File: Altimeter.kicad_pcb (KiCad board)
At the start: 4 copper layers, 37.5 x 25 mm, 99 parts, among them IC1 XTSD02GLGEAG, J1 Conn_01x04_Male, J2 Conn_01x02_Male, J3 USB_C_Receptacle_USB2.0, J4 Conn_01x02_Male, Q1 PMV20ENR, U1 150044M155220, U10 MAX77827AEFD+T, U11 SC4215, U2 ESP32-S3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

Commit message: 3rd iteration
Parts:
- added TP7: TestPoint, TestPoint:TestPoint_Pad_D1.0mm, B.Cu at (110.7, 97.8)
- USBLED1: footprint LED_SMD:LED_0603_1608Metric -> LED_SMD:LED_0402_1005Metric
- moved G*** 8.72 mm to (110.1, 90.9)
- moved USBLED1 8.01 mm to (128.3, 102.7), turned to 180 degrees
- moved TP5 3.57 mm to (106.4, 108.4)
- moved C14 3.19 mm to (107.0, 87.0), turned to 90 degrees
- moved R9 2.93 mm to (111.5, 89.5)
- moved R14 2.72 mm to (126.4, 102.7), turned to 0 degrees
- moved C13 2.39 mm to (110.9, 87.1)
- moved C1 2.19 mm to (103.7, 85.8), turned to 180 degrees
- moved TP9 1.98 mm to (108.7, 106.7)
- moved R8 1.96 mm to (105.6, 86.6)
- moved C7 1.58 mm to (107.0, 91.0), turned to -90 degrees
- moved C10 1.42 mm to (103.7, 92.5), turned to 0 degrees
- moved C8 1.15 mm to (107.1, 89.6), turned to 0 degrees
- moved R3 1.14 mm to (105.5, 92.5), turned to 180 degrees
- moved Y1 0.99 mm to (109.0, 87.2)
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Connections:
- C40 pad 2: Net-(IC1-VDD) -> GND
- IC1 pad 8: Net-(IC1-VDD) -> +3V3
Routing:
- net +3V3: track 37.6 -> 45.1 mm
- net VBUS: track 77.5 -> 72.9 mm
- net Net-(U2-MTMS/JTAG/GPIO42): track 4.26 -> 1.49 mm
- net Net-(USBLED1-A): track 3.43 -> 0.91 mm
- net /BOOT: track 7.09 -> 9.45 mm
- net GND: track 7.10 -> 9.09 mm, vias 42 -> 44
- net /power/BBIN: track 27.3 -> 29.3 mm
- net /TXD: track 3.52 -> 4.93 mm
- net Net-(IC1-CLK): track 5.48 -> 6.60 mm
- net /SCLK: track 36.1 -> 37.2 mm
- net Net-(IC1-VDD): track 1.03 -> 0.00 mm
- net Net-(U2-XTAL_N): track 6.00 -> 6.79 mm
- net Net-(C14-Pad1): track 2.37 -> 3.12 mm
- net /Data-: track 49.8 -> 49.1 mm
- net /MISO: track 31.9 -> 32.5 mm
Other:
- outline, holes or cut-outs redrawn
- board text added: "33L->"
- board text added: "3V3"
- board text added: "BBIN"
- board text added: "BBOUT"
- board text added: "CLK - IC"
- board text added: "CMD/DI - IC"
- board text added: "Dat+"
- board text added: "Dat-"
- board text added: "MISO"
- board text added: "MOSI"
- board text added: "RX"
- board text added: "SCLK"
- board text added: "SD0/DO - IC"
- board text added: "SD3/CS - IC"
- board text added: "TX"
- board text added: "USB"
- board text added: "VBUS"

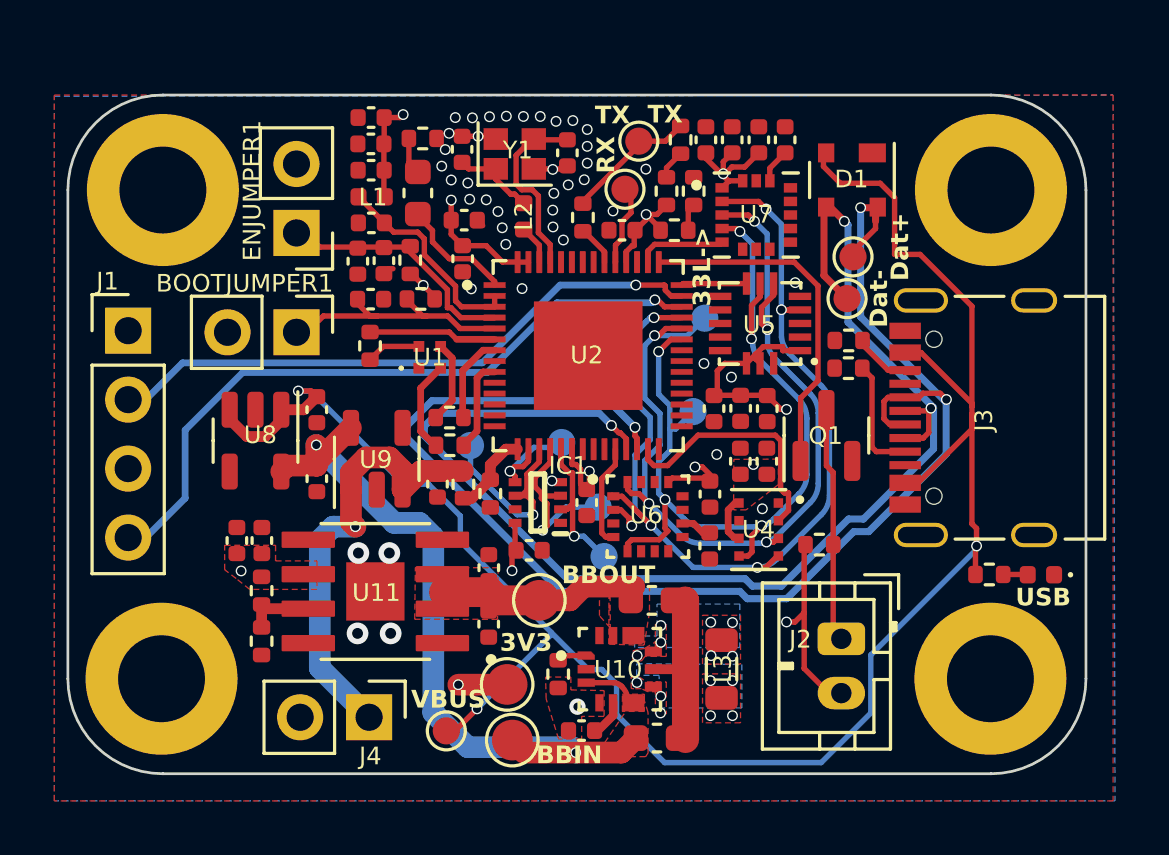
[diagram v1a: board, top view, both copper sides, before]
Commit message: 3rd iteration with new tracer spacing of 0.15
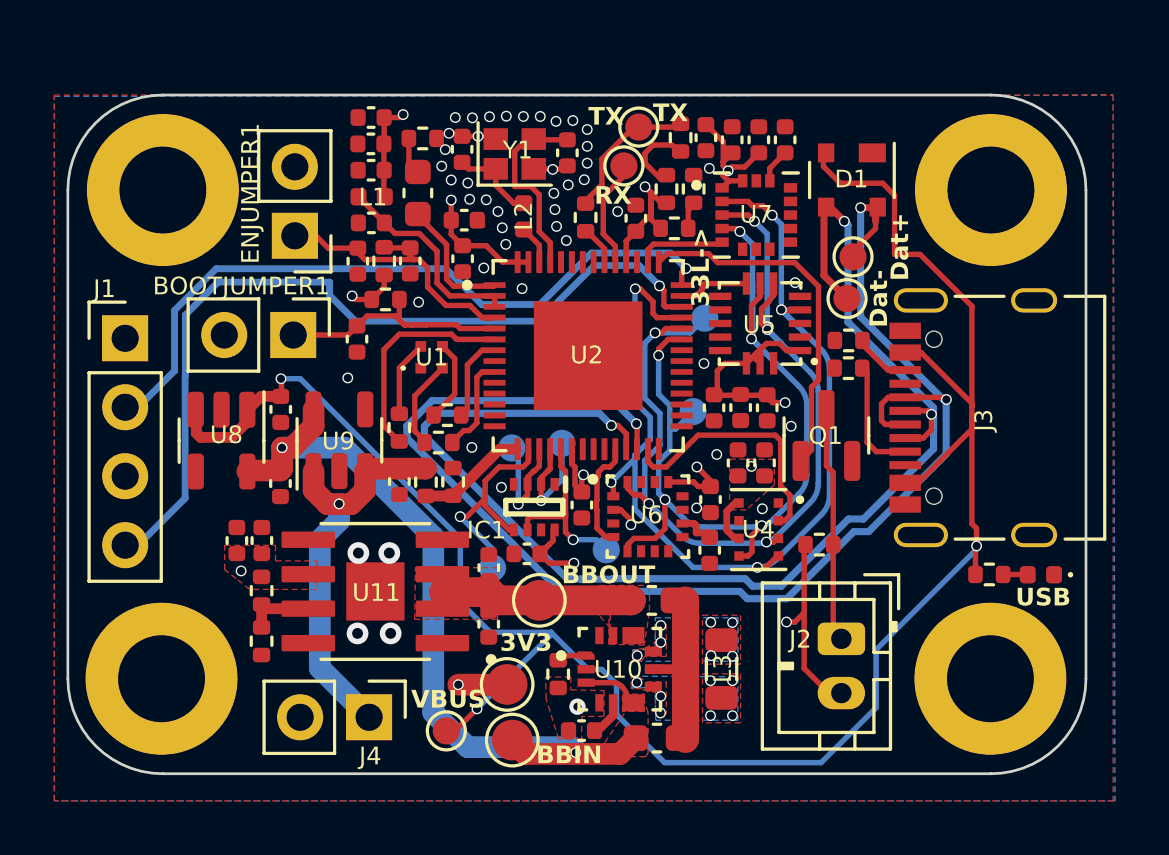
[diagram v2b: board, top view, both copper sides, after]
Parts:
- moved TP14 6.30 mm to (112.3, 101.8)
- moved TP7 5.28 mm to (108.1, 102.4)
- moved TP15 4.45 mm to (110.7, 97.8)
- moved TP13 3.86 mm to (108.8, 98.0)
- moved R5 3.20 mm to (104.7, 97.2), turned to -90 degrees
- moved C10 1.55 mm to (103.2, 94.0), turned to -90 degrees
- moved U9 1.53 mm to (102.5, 97.7)
- moved R15 1.44 mm to (106.7, 99.2), turned to 90 degrees
- moved C25 1.41 mm to (104.7, 99.2)
- moved R16 1.38 mm to (105.7, 99.3)
- moved C27 1.35 mm to (100.3, 99.3)
- moved C26 1.33 mm to (100.3, 96.6)
- moved R3 1.30 mm to (104.2, 92.5), turned to 0 degrees
- moved U8 1.25 mm to (98.2, 97.7)
- moved C2 0.97 mm to (105.1, 91.1)
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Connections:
- U2 pad 17: Net-(IC1-SD0/DO) -> Net-(IC1-CLK)
- U2 pad 18: Net-(IC1-CLK) -> Net-(IC1-SD3/CS)
- U2 pad 19: Net-(IC1-SD3/CS) -> Net-(IC1-SD0/DO)
- U2 pad 41: Net-(J1-Pin_2) -> /IMU/Accelerometer
- U2 pad 42: /IMU/Accelerometer -> Net-(J1-Pin_2)
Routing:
- net Net-(J1-Pin_4): track 25.2 -> 30.3 mm
- net +3V3: track 45.1 -> 49.9 mm
- net /MISO: track 32.5 -> 37.0 mm
- net Net-(IC1-CMD/DI): track 3.92 -> 8.27 mm
- net Net-(J1-Pin_2): track 21.8 -> 25.5 mm
- net Net-(U2-GPIO1/ADC1_CH0): track 4.70 -> 8.01 mm
- net /SCLK: track 37.2 -> 39.4 mm
- net Net-(IC1-CLK): track 6.60 -> 4.53 mm
- net Net-(J4-Pin_1): track 16.8 -> 14.9 mm
- net VBUS: track 72.9 -> 74.7 mm
- net Net-(TXLED1-A): track 1.09 -> 2.94 mm
- net /CHIP_PU: track 9.23 -> 10.6 mm
- net /power/BBIN: track 29.3 -> 30.7 mm
- net /RXD: track 3.01 -> 4.04 mm
- net /BattVolt: track 3.17 -> 4.03 mm
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
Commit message: hopefully final commit
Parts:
- C12: footprint Capacitor_SMD:C_0603_1608Metric -> Capacitor_SMD:C_0402_1005Metric
- moved G*** 1.65 mm to (109.0, 89.8)
- moved R8 0.70 mm to (105.1, 87.1), turned to -90 degrees
- moved C12 0.49 mm to (105.7, 89.0)
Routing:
- net GND: vias 48 -> 47
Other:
- board text added: "33L-"
- board text added: "BB IN"
- board text removed: "33L->"
- board text removed: "BBIN"
